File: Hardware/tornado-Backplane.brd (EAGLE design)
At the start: 122.1 x 128.1 mm, 13 parts, among them CON1 ROV_SHIELD_V2

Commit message: Wrapping up initial board layout
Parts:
- moved BRICKS_COM 18.7 mm to (62.6, 15.1)
- moved CON1 18.7 mm to (0.00, 0.50)
- moved EMPTY 18.7 mm to (61.6, 55.0)
- moved EMPTY2 18.7 mm to (61.3, 31.8)
- moved GPIO_GEN2 18.7 mm to (74.8, 14.6)
- moved GPIO_GENERIC 18.7 mm to (72.0, 55.4)
- moved IO_PUMP? 18.7 mm to (23.9, 26.0)
- moved NAV_POWER 18.7 mm to (22.8, 57.7)
- moved POWER_INPUT 18.7 mm to (39.2, 14.6)
- moved EMPTY3 18.7 mm to (22.9, 39.9)
- moved NAV_COM 18.7 mm to (22.9, 68.7)
- moved MAIN_CAMERA 18.7 mm to (61.8, 40.9)
- moved SOLENOID_SWITCH 18.7 mm to (61.2, 66.5)
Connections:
- removed net N$23: CON1.14
- new net SONAR_TIMER: BRICKS_COM.C2, CON1.14
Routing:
- net SONAR_TIMER: track 0.00 -> 13.8 mm
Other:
- board size 122.1 x 128.1 mm -> 84 x 84.5 mm
- board text added: "/home/sample/tornado-clip-art-9TRb5XqTe.bmp"

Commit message: Board Design Rev 1.0
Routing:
- net LED_PWM: track 36.9 -> 40.7 mm
- net SONAR_TIMER: track 13.8 -> 15.4 mm, vias 0 -> 1
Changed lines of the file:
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@@
 <?xml version="1.0" encoding="utf-8"?>
 <!DOCTYPE eagle SYSTEM "eagle.dtd">
-<eagle version="6.6.0">
+<eagle version="7.6.0">
 <drawing>
 <settings>
@@
 <setting verticaltext="up"/>
 </settings>
-<grid distance="0.7" unitdist="mil" unit="mil" style="lines" multiple="1" display="yes" altdistance="0.025" altunitdist="inch" altunit="inch"/>
+<grid distance="0.01778" unitdist="mm" unit="mm" style="lines" multiple="1" display="yes" altdistance="0.025" altunitdist="inch" altunit="mm"/>
 <layers>
 <layer number="1" name="Top" color="4" fill="1" visible="yes" active="yes"/>
@@
 </class>
 </classes>
-<designrules name="GoldPhoenix">
-<description language="en">
-&lt;b&gt;Gold Phoenix PCB Design Rules&lt;/b&gt;
+<designrules name="PCBs_io">
+<description language="de">&lt;b&gt;MakerWorks Design Rules&lt;/b&gt;
 &lt;p&gt;
-Created by Nick Molo for the Purdue IEEE ROV Team
-</description>
+Die Standard-Design-Rules sind so gewählt, dass sie für
+die meisten Anwendungen passen. Sollte ihre Platine
+besondere Anforderungen haben, treffen Sie die erforderlichen
+Einstellungen hier und speichern die Design Rules unter
+einem neuen Namen ab.</description>
+<description language="en">&lt;b&gt;MakerWorks Design Rules&lt;/b&gt;
+&lt;p&gt;
+Please ensure your boards meet these minimum design rule requirements.</description>
 <param name="layerSetup" value="(1*16)"/>
-<param name="mtCopper" value="0.035mm 0.035mm 0.035mm 0.035mm 0.035mm 0.035mm 0.035mm 0.035mm 0.035mm 0.035mm 0.035mm 0.035mm 0.035mm 0.035mm 0.035mm 0.035mm"/>
-<param name="mtIsolate" value="1.5mm 0.15mm 0.2mm 0.15mm 0.2mm 0.15mm 0.2mm 0.15mm 0.2mm 0.15mm 0.2mm 0.15mm 0.2mm 0.15mm 0.2mm"/>
-<param name="mdWireWire" value="7mil"/>
-<param name="mdWirePad" value="7mil"/>
-<param name="mdWireVia" value="7mil"/>
-<param name="mdPadPad" value="7mil"/>
-<param name="mdPadVia" value="7mil"/>
-<param name="mdViaVia" value="7mil"/>
-<param name="mdSmdPad" value="7mil"/>
-<param name="mdSmdVia" value="7mil"/>
-<param name="mdSmdSmd" value="7mil"/>
+<param name="mtCopper" value="0.0356mm 0.0356mm 0.0356mm 0.0356mm 0.0356mm 0.0356mm 0.0356mm 0.0356mm 0.0356mm 0.0356mm 0.0356mm 0.0356mm 0.0356mm 0.0356mm 0.0356mm 0.0356mm"/>
+<param name="mtIsolate" value="1.5011mm 0.1499mm 0.2007mm 0.1499mm 0.2007mm 0.1499mm 0.2007mm 0.1499mm 0.2007mm 0.1499mm 0.2007mm 0.1499mm 0.2007mm 0.1499mm 0.2007mm"/>
+<param name="mdWireWire" value="6mil"/>
+<param name="mdWirePad" value="6mil"/>
+<param name="mdWireVia" value="6mil"/>
+<param name="mdPadPad" value="6mil"/>
+<param name="mdPadVia" value="6mil"/>
+<param name="mdViaVia" value="6mil"/>
+<param name="mdSmdPad" value="6mil"/>
+<param name="mdSmdVia" value="6mil"/>
+<param name="mdSmdSmd" value="6mil"/>
 <param name="mdViaViaSameLayer" value="8mil"/>
 <param name="mnLayersViaInSmd" value="2"/>
-<param name="mdCopperDimension" value="10mil"/>
-<param name="mdDrill" value="8mil"/>
+<param name="mdCopperDimension" value="15mil"/>
+<param name="mdDrill" value="6mil"/>
 <param name="mdSmdStop" value="0mil"/>
-<param name="msWidth" value="7mil"/>
-<param name="msDrill" value="10mil"/>
-<param name="msMicroVia" value="9.99mm"/>
+<param name="msWidth" value="6mil"/>
+<param name="msDrill" value="13mil"/>
+<param name="msMicroVia" value="13mil"/>
 <param name="msBlindViaRatio" value="0.5"/>
 <param name="rvPadTop" value="0.25"/>
@@
 <param name="rvMicroViaOuter" value="0.25"/>
 <param name="rvMicroViaInner" value="0.25"/>
-<param name="rlMinPadTop" value="10mil"/>
+<param name="rlMinPadTop" value="7mil"/>
 <param name="rlMaxPadTop" value="20mil"/>
-<param name="rlMinPadInner" value="10mil"/>
+<param name="rlMinPadInner" value="7mil"/>
 <param name="rlMaxPadInner" value="20mil"/>
-<param name="rlMinPadBottom" value="10mil"/>
+<param name="rlMinPadBottom" value="7mil"/>
 <param name="rlMaxPadBottom" value="20mil"/>
-<param name="rlMinViaOuter" value="10mil"/>
+<param name="rlMinViaOuter" value="7mil"/>
 <param name="rlMaxViaOuter" value="20mil"/>
-<param name="rlMinViaInner" value="10mil"/>
+<param name="rlMinViaInner" value="7mil"/>
 <param name="rlMaxViaInner" value="20mil"/>
 <param name="rlMinMicroViaOuter" value="4mil"/>
@@
 <param name="mvStopFrame" value="1"/>
 <param name="mvCreamFrame" value="0"/>
-<param name="mlMinStopFrame" value="4mil"/>
-<param name="mlMaxStopFrame" value="4mil"/>
+<param name="mlMinStopFrame" value="3mil"/>
+<param name="mlMaxStopFrame" value="3mil"/>
 <param name="mlMinCreamFrame" value="0mil"/>
 <param name="mlMaxCreamFrame" value="0mil"/>
-<param name="mlViaStopLimit" value="25mil"/>
+<param name="mlViaStopLimit" value="0mil"/>
 <param name="srRoundness" value="0"/>
 <param name="srMinRoundness" value="0mil"/>
@@
 <pass name="Default">
 <param name="RoutingGrid" value="50mil"/>
+<param name="AutoGrid" value="1"/>
+<param name="Efforts" value="0"/>
+<param name="TopRouterVariant" value="1"/>
 <param name="tpViaShape" value="round"/>
 <param name="PrefDir.1" value="|"/>
@@
 <contactref element="BRICKS_COM" pad="C3"/>
 <contactref element="CON1" pad="20"/>
-<wire x1="50.971725" y1="19.0378375" x2="50.971725" y2="16.971725" width="0.4064" layer="16"/>
-<wire x1="50.971725" y1="16.971725" x2="46" y2="12" width="0.4064" layer="16"/>
-<wire x1="46" y1="12" x2="40.9" y2="12" width="0.4064" layer="16"/>
-<wire x1="40.9" y1="12" x2="37.75" y2="8.85" width="0.4064" layer="16"/>
+<wire x1="50.971725" y1="19.0378375" x2="50.971725" y2="16.651684375" width="0.4064" layer="16"/>
+<wire x1="47.2446" y1="12.924559375" x2="41.824559375" y2="12.924559375" width="0.4064" layer="16"/>
+<wire x1="50.971725" y1="16.651684375" x2="47.2446" y2="12.924559375" width="0.4064" layer="16"/>
+<wire x1="41.824559375" y1="12.924559375" x2="37.75" y2="8.85" width="0.4064" layer="16"/>
 </signal>
 <signal name="MAIN_SERVO">
@@
 <signal name="LED_PWM">
 <contactref element="MAIN_CAMERA" pad="C3"/>
-<wire x1="50.17883125" y1="44.81239375" x2="50.17883125" y2="52.82116875" width="0.4064" layer="16"/>
-<wire x1="50.17883125" y1="52.82116875" x2="37.5" y2="65.5" width="0.4064" layer="16"/>
-<via x="37.5" y="65.5" extent="1-16" drill="0.6"/>
-<wire x1="37.5" y1="65.5" x2="37.5" y2="76.06" width="0.4064" layer="1"/>
 <contactref element="CON1" pad="79"/>
-<wire x1="37.75" y1="76.31" x2="37.5" y2="76.06" width="0.4064" layer="1"/>
+<wire x1="37.75" y1="76.31" x2="37.75" y2="53.7281" width="0.6096" layer="1"/>
+<wire x1="37.75" y1="53.7281" x2="40.60951875" y2="50.86858125" width="0.6096" layer="1"/>
+<via x="40.60951875" y="50.86858125" extent="1-16" drill="0.6"/>
+<wire x1="40.60951875" y1="50.86858125" x2="47.579278125" y2="50.86858125" width="0.6096" layer="16"/>
+<wire x1="47.579278125" y1="50.86858125" x2="50.175159375" y2="48.2727" width="0.6096" layer="16"/>
+<wire x1="50.175159375" y1="48.2727" x2="50.175159375" y2="44.816065625" width="0.6096" layer="16"/>
+<wire x1="50.175159375" y1="44.816065625" x2="50.17883125" y2="44.81239375" width="0.6096" layer="16"/>
 </signal>
 <signal name="GPIO">
@@
 <wire x1="35.21" y1="76.31" x2="35" y2="76.1" width="0.4064" layer="16"/>
 <wire x1="35" y1="76.1" x2="35" y2="74" width="0.4064" layer="16"/>
-<wire x1="35" y1="74" x2="40.5" y2="68.5" width="0.4064" layer="16"/>
-<wire x1="40.5" y1="68.5" x2="51" y2="68.5" width="0.4064" layer="16"/>
-<wire x1="51" y1="68.5" x2="52.611728125" y2="70.111728125" width="0.4064" layer="16"/>
+<wire x1="40.517778125" y1="68.731140625" x2="41.08958125" y2="68.731140625" width="0.4064" layer="16"/>
+<wire x1="41.08958125" y1="68.731140625" x2="51.017778125" y2="68.731140625" width="0.4064" layer="16"/>
 <wire x1="52.611728125" y1="70.111728125" x2="52.611728125" y2="70.475834375" width="0.4064" layer="16"/>
+<wire x1="51.017778125" y1="68.731140625" x2="52.611728125" y2="70.325090625" width="0.4064" layer="16"/>
+<wire x1="52.611728125" y1="70.325090625" x2="52.611728125" y2="70.475834375" width="0.4064" layer="16"/>
+<wire x1="35" y1="74" x2="40.268859375" y2="68.731140625" width="0.4064" layer="16"/>
+<wire x1="40.268859375" y1="68.731140625" x2="40.517778125" y2="68.731140625" width="0.4064" layer="16"/>
 </signal>
 <signal name="GPIO3">
@@
 <contactref element="BRICKS_COM" pad="C2"/>
 <contactref element="CON1" pad="14"/>
-<wire x1="53.971725" y1="19.0378375" x2="53.971725" y2="17.451725" width="0.4064" layer="16"/>
-<wire x1="53.971725" y1="17.451725" x2="45.37" y2="8.85" width="0.4064" layer="16"/>
+<wire x1="53.971725" y1="19.0378375" x2="53.971725" y2="18.544540625" width="0.4064" layer="16"/>
+<wire x1="53.971725" y1="18.544540625" x2="53.971725" y2="17.451725" width="0.4064" layer="16"/>
+<wire x1="45.37" y1="8.85" x2="51.0996" y2="14.5796" width="0.4064" layer="1"/>
+<wire x1="51.0996" y1="14.5796" x2="53.926740625" y2="14.5796" width="0.4064" layer="1"/>
+<via x="53.926740625" y="14.5796" extent="1-16" drill="0.6"/>
+<wire x1="53.926740625" y1="14.5796" x2="53.971725" y2="14.624584375" width="0.4064" layer="16"/>
+<wire x1="53.971725" y1="14.624584375" x2="53.971725" y2="17.451725" width="0.4064" layer="16"/>
 </signal>
 </signals>

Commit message: Post Nick recomendations
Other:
- board text added: "Board made by Sam Deghuee and Flor Albornoz, with help from Matt Molo Purdue ROV 2016"
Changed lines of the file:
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@@
 <layer number="25" name="tNames" color="7" fill="1" visible="yes" active="yes"/>
 <layer number="26" name="bNames" color="7" fill="1" visible="yes" active="yes"/>
-<layer number="27" name="tValues" color="7" fill="1" visible="no" active="yes"/>
+<layer number="27" name="tValues" color="7" fill="1" visible="yes" active="yes"/>
 <layer number="28" name="bValues" color="7" fill="1" visible="no" active="yes"/>
 <layer number="29" name="tStop" color="7" fill="3" visible="no" active="yes"/>
@@
 <rectangle x1="11.05026875" y1="21.75383125" x2="11.10360625" y2="21.77160625" layer="21"/>
 <text x="0" y="-0.0889" size="0.035559375" layer="21" font="vector">/home/sample/tornado-clip-art-9TRb5XqTe.bmp</text>
+<text x="63.5635" y="4.498340625" size="1.016" layer="27">Board made by Sam Deghuee
+and Flor Albornoz,
+with help from Matt Molo
+Purdue ROV 2016</text>
 </plain>
 <attributes>
@@
 </board>
 </drawing>
+<compatibility>
+<note version="6.3" minversion="6.2.2" severity="warning">
+Since Version 6.2.2 text objects can contain more than one line,
+which will not be processed correctly with this version.
+</note>
+</compatibility>
 </eagle>

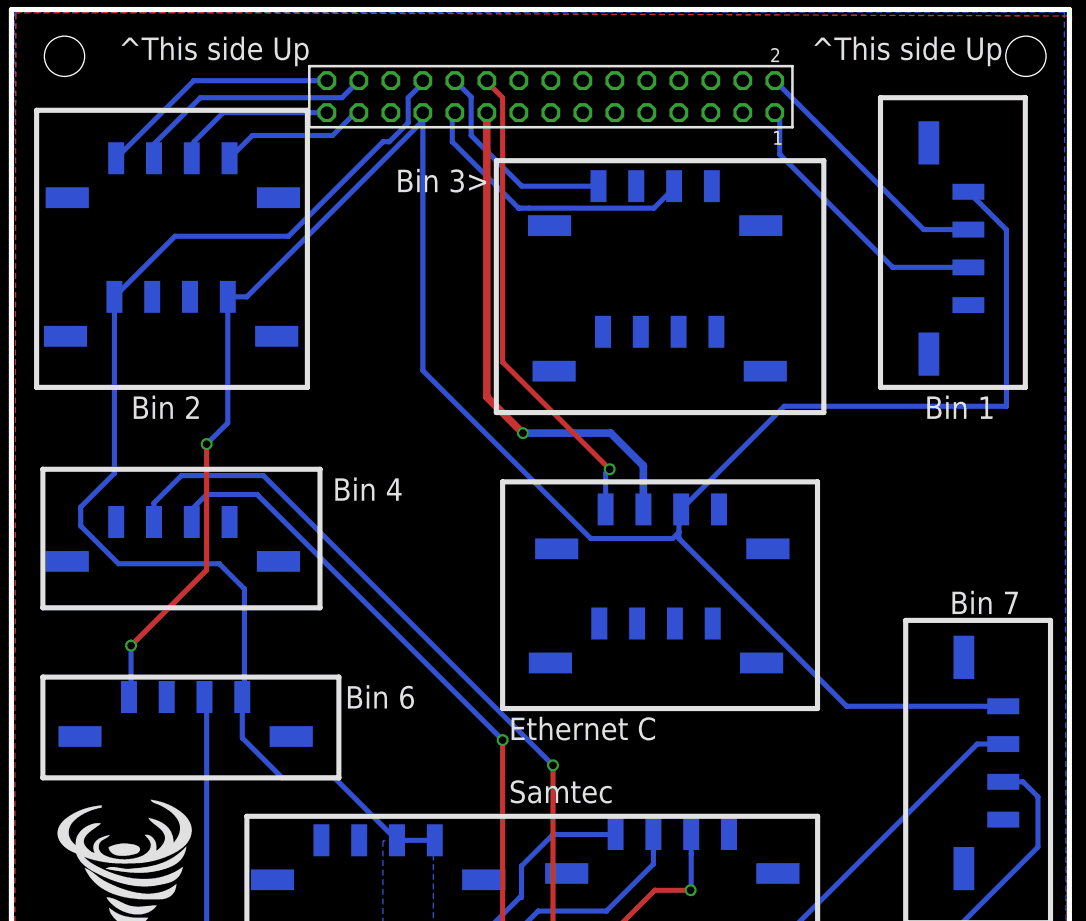
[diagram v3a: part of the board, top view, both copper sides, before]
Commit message: Fixes from Michael
Mostly layout, fixing ground islands, and other small fixes.
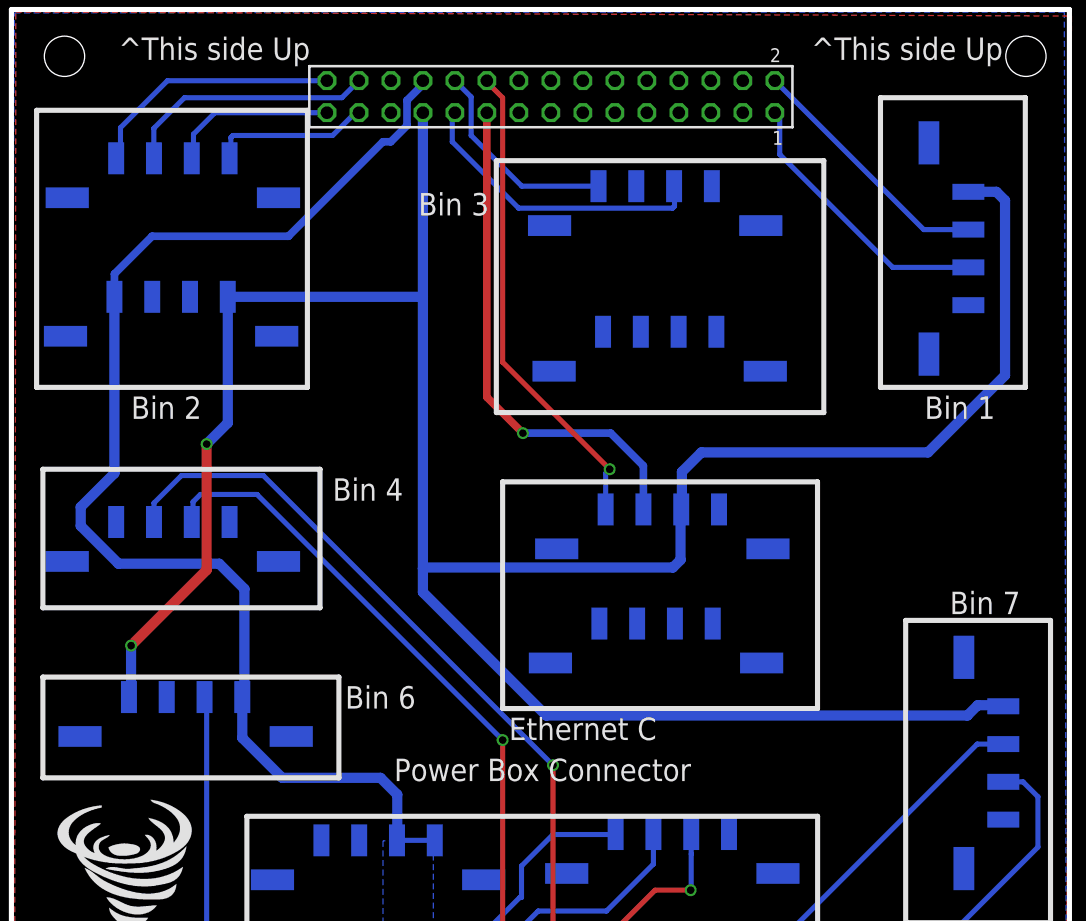
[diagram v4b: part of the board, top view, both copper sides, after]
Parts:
- gave numbers to parts that had none: 1
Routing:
- net +5V: track 184.0 -> 213.5 mm
- net +12V: track 97.8 -> 101.3 mm
- net NAV_SDA: track 19.5 -> 20.7 mm
- net SONAR_PWM: track 19.3 -> 20.5 mm
- net SOL_O2: track 23.4 -> 24.4 mm
- net SONAR_DAC: track 11.8 -> 12.7 mm
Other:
- board text added: "Bin 3"
- board text added: "Power Box Connector"
- board text removed: "Bin 3>"
- board text removed: "Samtec"
